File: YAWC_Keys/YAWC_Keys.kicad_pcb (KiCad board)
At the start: 2 copper layers, 99 x 97 mm, 19 parts, among them P1 K1, P10 K10, P11 K11, P2 K2, P3 K3, P4 K4, P5 K5, P6 K6, P7 K7, P8 K8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

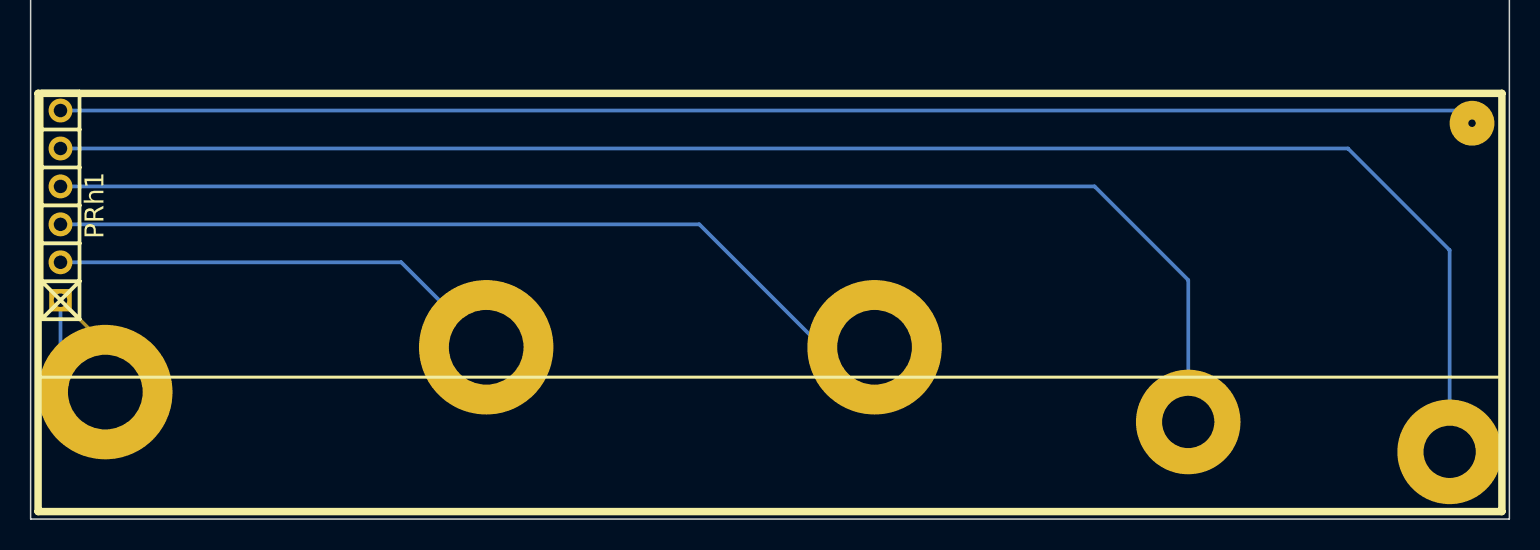
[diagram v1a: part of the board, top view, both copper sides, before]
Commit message: Possition centre lines and connectors
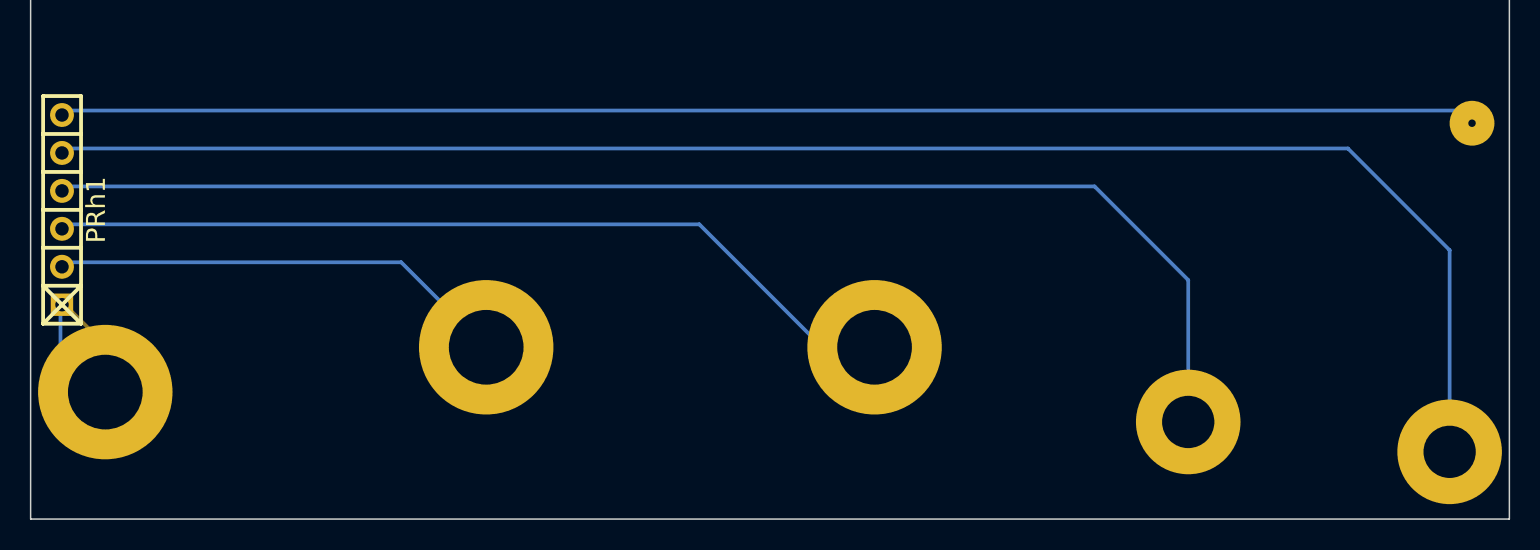
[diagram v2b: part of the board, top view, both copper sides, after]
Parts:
- moved PRh1 0.32 mm to (37.6, 112.8)
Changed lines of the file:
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@@
   )
   (module PIN_Hdr:Pin_Header_1x06 (layer F.Cu)
-    (at 37.5 112.5 90)
+    (at 37.6 112.8 90)
     (descr "1 pin")
     (tags "CONN DEV")
@@
   (gr_line (start 35.5 36.5) (end 134.5 36.5) (angle 90) (layer Edge.Cuts) (width 0.1))
   (gr_line (start 35.5 133.5) (end 35.5 36.5) (angle 90) (layer Edge.Cuts) (width 0.1))
-  (gr_line (start 36 85) (end 133.5 85) (angle 90) (layer B.SilkS) (width 0.3))
+  (gr_line (start 36 87.5) (end 133.5 87.5) (angle 90) (layer B.SilkS) (width 0.3))
   (gr_line (start 134 37) (end 36 37) (angle 90) (layer B.SilkS) (width 0.5))
   (gr_line (start 134 65) (end 134 37) (angle 90) (layer B.SilkS) (width 0.5))
   (gr_line (start 36 65) (end 134 65) (angle 90) (layer B.SilkS) (width 0.5))
   (gr_line (start 36 37) (end 36 65) (angle 90) (layer B.SilkS) (width 0.5))
-  (gr_line (start 36 133) (end 36 105) (angle 90) (layer F.SilkS) (width 0.5))
-  (gr_line (start 134 133) (end 36 133) (angle 90) (layer F.SilkS) (width 0.5))
-  (gr_line (start 134 105) (end 134 133) (angle 90) (layer F.SilkS) (width 0.5))
-  (gr_line (start 36 105) (end 134 105) (angle 90) (layer F.SilkS) (width 0.5))
+  (gr_line (start 36 133) (end 36 105) (angle 90) (layer B.SilkS) (width 0.5))
+  (gr_line (start 134 133) (end 36 133) (angle 90) (layer B.SilkS) (width 0.5))
+  (gr_line (start 134 105) (end 134 133) (angle 90) (layer B.SilkS) (width 0.5))
+  (gr_line (start 36 105) (end 134 105) (angle 90) (layer B.SilkS) (width 0.5))
   (gr_line (start 134 71) (end 36 71) (angle 90) (layer B.SilkS) (width 0.5))
   (gr_line (start 134 99) (end 134 71) (angle 90) (layer B.SilkS) (width 0.5))
@@
     (effects (font (size 5 5) (thickness 0.3)) (justify mirror))
   )
-  (gr_line (start 36 124) (end 134 124) (angle 90) (layer F.SilkS) (width 0.2))
-  (gr_line (start 36 51) (end 134 51) (angle 90) (layer B.SilkS) (width 0.2))
+  (gr_line (start 36 121.5) (end 134 121.5) (angle 90) (layer B.SilkS) (width 0.2))
+  (gr_line (start 36 53.5) (end 134 53.5) (angle 90) (layer B.SilkS) (width 0.2))
   (segment (start 132 63.08) (end 52.58 63.08) (width 0.25) (layer B.Cu) (net 1))
   (segment (start 52.58 63.08) (end 40.5 51) (width 0.25) (layer B.Cu) (net 1))

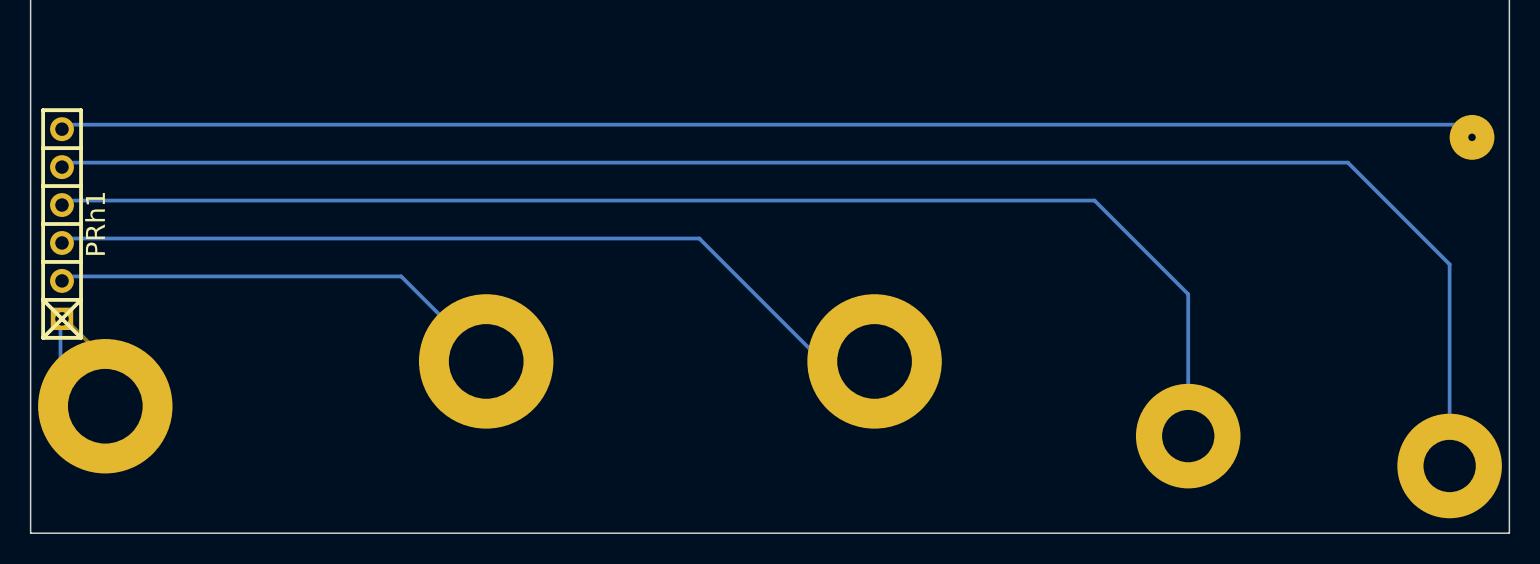
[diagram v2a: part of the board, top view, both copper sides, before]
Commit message: Correct center lines again
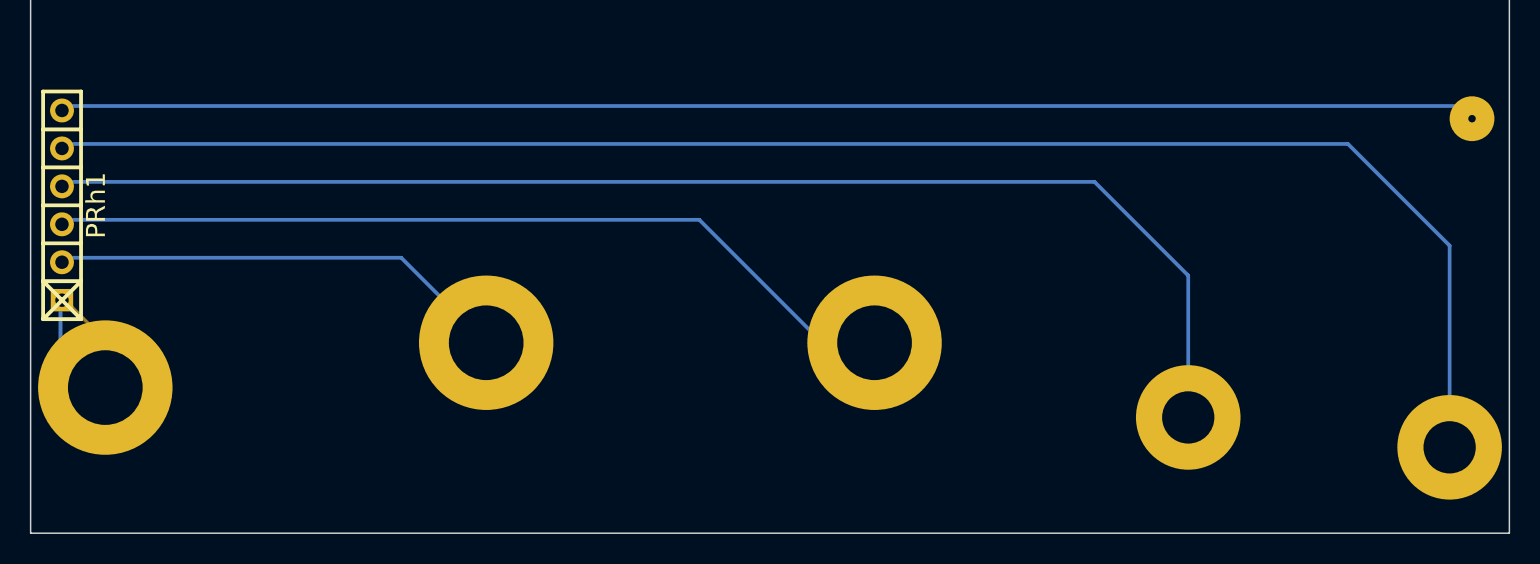
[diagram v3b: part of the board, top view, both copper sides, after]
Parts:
- moved P10 1.25 mm to (130.5, 127.8)
- moved P11 1.25 mm to (132.0, 105.8)
- moved P6 1.25 mm to (40.5, 123.8)
- moved P7 1.25 mm to (66.0, 120.8)
- moved P8 1.25 mm to (92.0, 120.8)
- moved P9 1.25 mm to (113.0, 125.8)
- moved PRh1 1.25 mm to (37.6, 111.5)
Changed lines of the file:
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@@
   )
   (module PIN_Hdr:RndKeyCon5 (layer F.Cu)
-    (at 40.5 125)
+    (at 40.5 123.75)
     (fp_text reference P6 (at 0.7 5.4) (layer F.SilkS) hide
       (effects (font (size 1 1) (thickness 0.15)))
@@
   )
   (module PIN_Hdr:RndKeyCon5 (layer F.Cu)
-    (at 66 122)
+    (at 66 120.75)
     (fp_text reference P7 (at 0.7 5.4) (layer F.SilkS) hide
       (effects (font (size 1 1) (thickness 0.15)))
@@
   )
   (module PIN_Hdr:RndKeyCon5 (layer F.Cu)
-    (at 92 122)
+    (at 92 120.75)
     (fp_text reference P8 (at 0.7 5.4) (layer F.SilkS) hide
       (effects (font (size 1 1) (thickness 0.15)))
@@
   )
   (module PIN_Hdr:TabKey3_5 (layer F.Cu)
-    (at 113 127)
+    (at 113 125.75)
     (fp_text reference P9 (at 0.5 4.6) (layer F.SilkS) hide
       (effects (font (size 1 1) (thickness 0.15)))
@@
   )
   (module PIN_Hdr:TabKey3_5 (layer F.Cu)
-    (at 130.5 129)
+    (at 130.5 127.75)
     (fp_text reference P10 (at 0.5 4.6) (layer F.SilkS) hide
       (effects (font (size 1 1) (thickness 0.15)))
@@
   )
   (module PIN_Hdr:TabKey3_5 (layer F.Cu)
-    (at 132 107)
+    (at 132 105.75)
     (fp_text reference P11 (at 0.5 4.6) (layer F.SilkS) hide
       (effects (font (size 1 1) (thickness 0.15)))
@@
   )
   (module PIN_Hdr:Pin_Header_1x06 (layer F.Cu)
-    (at 37.6 112.8 90)
+    (at 37.6 111.55 90)
     (descr "1 pin")
     (tags "CONN DEV")
@@
   (gr_line (start 36 65) (end 134 65) (angle 90) (layer B.SilkS) (width 0.5))
   (gr_line (start 36 37) (end 36 65) (angle 90) (layer B.SilkS) (width 0.5))
-  (gr_line (start 36 133) (end 36 105) (angle 90) (layer B.SilkS) (width 0.5))
-  (gr_line (start 134 133) (end 36 133) (angle 90) (layer B.SilkS) (width 0.5))
-  (gr_line (start 134 105) (end 134 133) (angle 90) (layer B.SilkS) (width 0.5))
-  (gr_line (start 36 105) (end 134 105) (angle 90) (layer B.SilkS) (width 0.5))
+  (gr_line (start 36 131.75) (end 36 103.75) (angle 90) (layer B.SilkS) (width 0.5))
+  (gr_line (start 134 131.75) (end 36 131.75) (angle 90) (layer B.SilkS) (width 0.5))
+  (gr_line (start 134 103.75) (end 134 131.75) (angle 90) (layer B.SilkS) (width 0.5))
+  (gr_line (start 36 103.75) (end 134 103.75) (angle 90) (layer B.SilkS) (width 0.5))
   (gr_line (start 134 71) (end 36 71) (angle 90) (layer B.SilkS) (width 0.5))
   (gr_line (start 134 99) (end 134 71) (angle 90) (layer B.SilkS) (width 0.5))
   (gr_line (start 36 99) (end 134 99) (angle 90) (layer B.SilkS) (width 0.5))
   (gr_line (start 36 71) (end 36 99) (angle 90) (layer B.SilkS) (width 0.5))
-  (gr_text Right (at 86 112 180) (layer B.SilkS)
+  (gr_text Right (at 86 110.75 180) (layer B.SilkS)
     (effects (font (size 5 5) (thickness 0.3)) (justify mirror))
   )
@@
     (effects (font (size 5 5) (thickness 0.3)) (justify mirror))
   )
-  (gr_line (start 36 121.5) (end 134 121.5) (angle 90) (layer B.SilkS) (width 0.2))
-  (gr_line (start 36 53.5) (end 134 53.5) (angle 90) (layer B.SilkS) (width 0.2))
+  (gr_line (start 36 120.25) (end 134 120.25) (angle 90) (layer B.SilkS) (width 0.2))
+  (gr_line (start 36 48.5) (end 134 48.5) (angle 90) (layer B.SilkS) (width 0.2))
   (segment (start 132 63.08) (end 52.58 63.08) (width 0.25) (layer B.Cu) (net 1))
   (segment (start 52.58 63.08) (end 40.5 51) (width 0.25) (layer B.Cu) (net 1))
@@
   (segment (start 129 47) (end 129 49.92) (width 0.25) (layer B.Cu) (net 5))
   (segment (start 129 49.92) (end 132 52.92) (width 0.25) (layer B.Cu) (net 5))
-  (segment (start 37.5 118.85) (end 37.5 122) (width 0.25) (layer B.Cu) (net 6))
-  (segment (start 37.5 122) (end 40.5 125) (width 0.25) (layer B.Cu) (net 6))
-  (segment (start 40.5 125) (end 40.5 121.85) (width 0.25) (layer F.Cu) (net 6))
-  (segment (start 40.5 121.85) (end 37.5 118.85) (width 0.25) (layer F.Cu) (net 6))
-  (segment (start 37.5 116.31) (end 60.31 116.31) (width 0.25) (layer B.Cu) (net 7))
-  (segment (start 60.31 116.31) (end 66 122) (width 0.25) (layer B.Cu) (net 7))
-  (segment (start 92 122) (end 88.5 122) (width 0.25) (layer B.Cu) (net 8))
-  (segment (start 88.5 122) (end 80.27 113.77) (width 0.25) (layer B.Cu) (net 8))
-  (segment (start 80.27 113.77) (end 37.5 113.77) (width 0.25) (layer B.Cu) (net 8))
-  (segment (start 37.5 111.23) (end 106.73 111.23) (width 0.25) (layer B.Cu) (net 9))
-  (segment (start 113 117.5) (end 113 127) (width 0.25) (layer B.Cu) (net 9))
-  (segment (start 106.73 111.23) (end 113 117.5) (width 0.25) (layer B.Cu) (net 9))
-  (segment (start 37.5 108.69) (end 123.69 108.69) (width 0.25) (layer B.Cu) (net 10))
-  (segment (start 130.5 115.5) (end 130.5 129) (width 0.25) (layer B.Cu) (net 10))
-  (segment (start 123.69 108.69) (end 130.5 115.5) (width 0.25) (layer B.Cu) (net 10))
-  (segment (start 37.5 106.15) (end 131.15 106.15) (width 0.25) (layer B.Cu) (net 11))
-  (segment (start 131.15 106.15) (end 132 107) (width 0.25) (layer B.Cu) (net 11))
-  (segment (start 131.15 106.15) (end 132 107) (width 0.25) (layer F.Cu) (net 11))
+  (segment (start 37.5 117.6) (end 37.5 120.75) (width 0.25) (layer B.Cu) (net 6))
+  (segment (start 37.5 120.75) (end 40.5 123.75) (width 0.25) (layer B.Cu) (net 6))
+  (segment (start 40.5 123.75) (end 40.5 120.6) (width 0.25) (layer F.Cu) (net 6))
+  (segment (start 40.5 120.6) (end 37.5 117.6) (width 0.25) (layer F.Cu) (net 6))
+  (segment (start 37.5 115.06) (end 60.31 115.06) (width 0.25) (layer B.Cu) (net 7))
+  (segment (start 60.31 115.06) (end 66 120.75) (width 0.25) (layer B.Cu) (net 7))
+  (segment (start 92 120.75) (end 88.5 120.75) (width 0.25) (layer B.Cu) (net 8))
+  (segment (start 88.5 120.75) (end 80.27 112.52) (width 0.25) (layer B.Cu) (net 8))
+  (segment (start 80.27 112.52) (end 37.5 112.52) (width 0.25) (layer B.Cu) (net 8))
+  (segment (start 37.5 109.98) (end 106.73 109.98) (width 0.25) (layer B.Cu) (net 9))
+  (segment (start 113 116.25) (end 113 125.75) (width 0.25) (layer B.Cu) (net 9))
+  (segment (start 106.73 109.98) (end 113 116.25) (width 0.25) (layer B.Cu) (net 9))
+  (segment (start 37.5 107.44) (end 123.69 107.44) (width 0.25) (layer B.Cu) (net 10))
+  (segment (start 130.5 114.25) (end 130.5 127.75) (width 0.25) (layer B.Cu) (net 10))
+  (segment (start 123.69 107.44) (end 130.5 114.25) (width 0.25) (layer B.Cu) (net 10))
+  (segment (start 37.5 104.9) (end 131.15 104.9) (width 0.25) (layer B.Cu) (net 11))
+  (segment (start 131.15 104.9) (end 132 105.75) (width 0.25) (layer B.Cu) (net 11))
+  (segment (start 131.15 104.9) (end 132 105.75) (width 0.25) (layer F.Cu) (net 11))
   (segment (start 123 82.58) (end 123 83) (width 0.25) (layer B.Cu) (net 12))
   (segment (start 123 83) (end 119 87) (width 0.25) (layer B.Cu) (net 12))

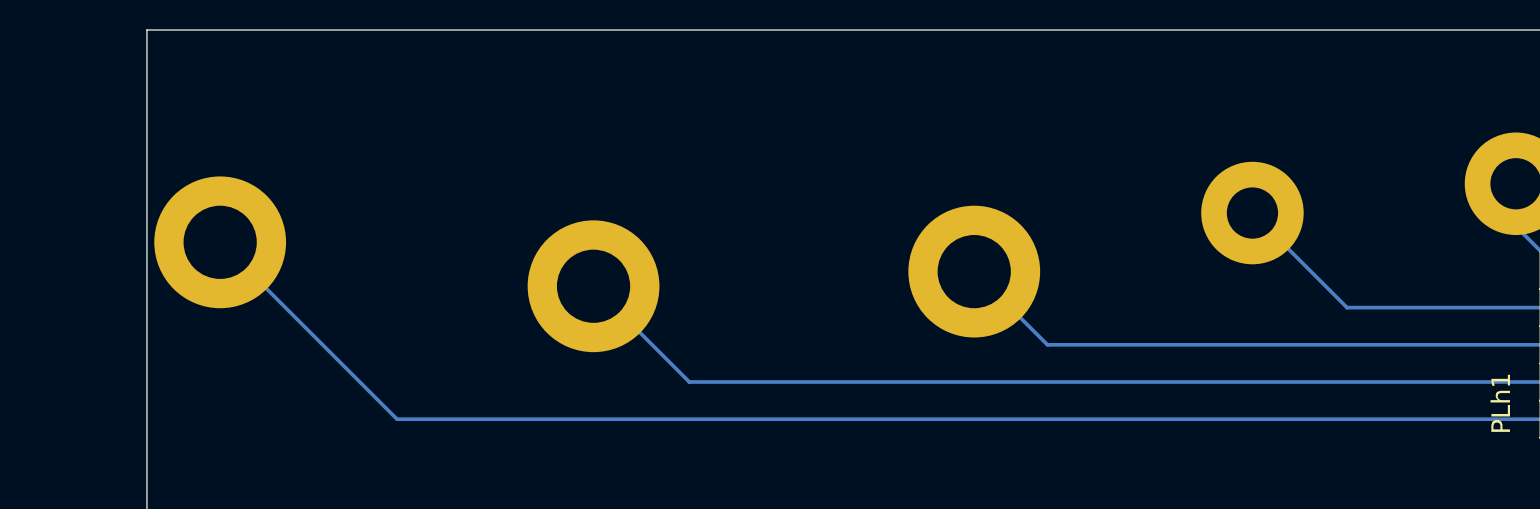
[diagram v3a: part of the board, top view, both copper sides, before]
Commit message: Add route plugs for breath amp through to main board via keys. Add straight 1x6 header
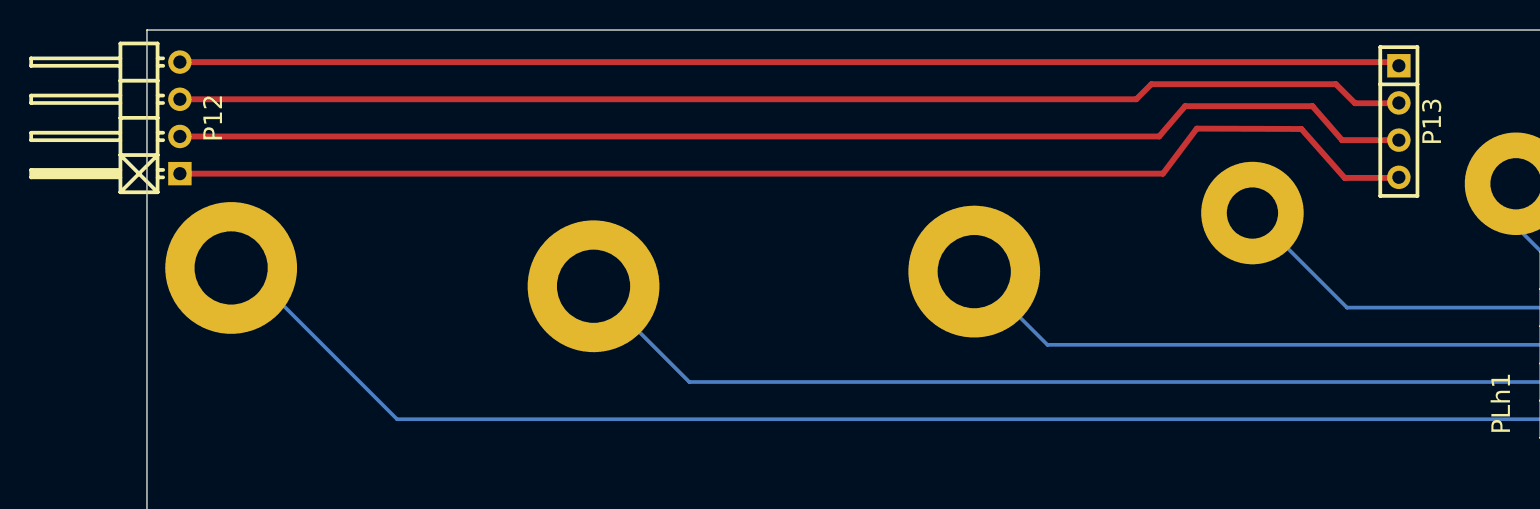
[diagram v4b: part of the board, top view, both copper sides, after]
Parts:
- added P12: CONN_01X04, My_Pin_Headers:Pin_Header_Angled_1x04, F.Cu at (37.8, 42.5)
- added P13: CONN_01X04, My_Pin_Headers:Pin_Header_Straight_1x04, F.Cu at (121.0, 42.8)
- moved P1 1.90 mm to (41.2, 52.8)
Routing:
- net /Bite: track 0.00 -> 86.3 mm
- net /Breath: track 0.00 -> 85.3 mm
- net /+ve: track 0.00 -> 84.2 mm
- net /Gnd: track 0.00 -> 83.4 mm
- net Net-(P1-Pad1): track 100.5 -> 99.0 mm
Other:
- net class CirTrack added: clearance 0.2, trace_width 0.4, via_dia 0.6, via_drill 0.4
